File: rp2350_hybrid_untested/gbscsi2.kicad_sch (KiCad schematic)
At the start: 154 parts, among them J1 USB_DATA, J2 TF003, J3 Conn_01x02, J4 Conn_01x04, J5 SCSI_50-2P_2mm, J6 SCSI_50P_2.54mm, J7 Conn_01x04, Q1 AO3401A, Q10 AO3401A, Q11 AO3401A, Q12 AO3401A, Q13 AO3401A, Q14 AO3401A, Q15 AO3401A, Q16 AO3401A, Q17 AO3401A, Q18 AO3401A, Q2 AO3401A, Q3 AO3401A, Q4 AO3401A, Q5 AO3401A, Q6 AO3401A, Q7 AO3401A, Q8 AO3401A, Q9 AO3401A, SW1 SW_DIP_x04, U1 RP2350_60QFN, U2 W25Q128JVS, U4 74AHCT1G125, U7 AZ1117-2.85, U8 AP62250WU, U9 USB TVS, Y1 12MHz

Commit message: Changed diodes in BoM, minor corrections to PCB, documentation
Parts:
- D? (x4): LCSC C8598 -> C82544
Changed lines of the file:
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@@
       (effects (font (size 1.27 1.27)))
     )
-    (property "LCSC" "C8598" (at 281.94 27.94 0)
+    (property "LCSC" "C82544" (at 281.94 27.94 0)
       (effects (font (size 1.27 1.27)) hide)
     )
@@
       (effects (font (size 1.27 1.27)))
     )
-    (property "LCSC" "C8598" (at 274.32 35.56 0)
+    (property "LCSC" "C82544" (at 274.32 35.56 0)
       (effects (font (size 1.27 1.27)) hide)
     )
@@
       (effects (font (size 1.27 1.27)))
     )
-    (property "LCSC" "C8598" (at 281.94 57.15 0)
+    (property "LCSC" "C82544" (at 281.94 57.15 0)
       (effects (font (size 1.27 1.27)) hide)
     )
@@
       (effects (font (size 1.27 1.27)))
     )
-    (property "LCSC" "C8598" (at 281.94 66.04 0)
+    (property "LCSC" "C82544" (at 281.94 66.04 0)
       (effects (font (size 1.27 1.27)) hide)
     )

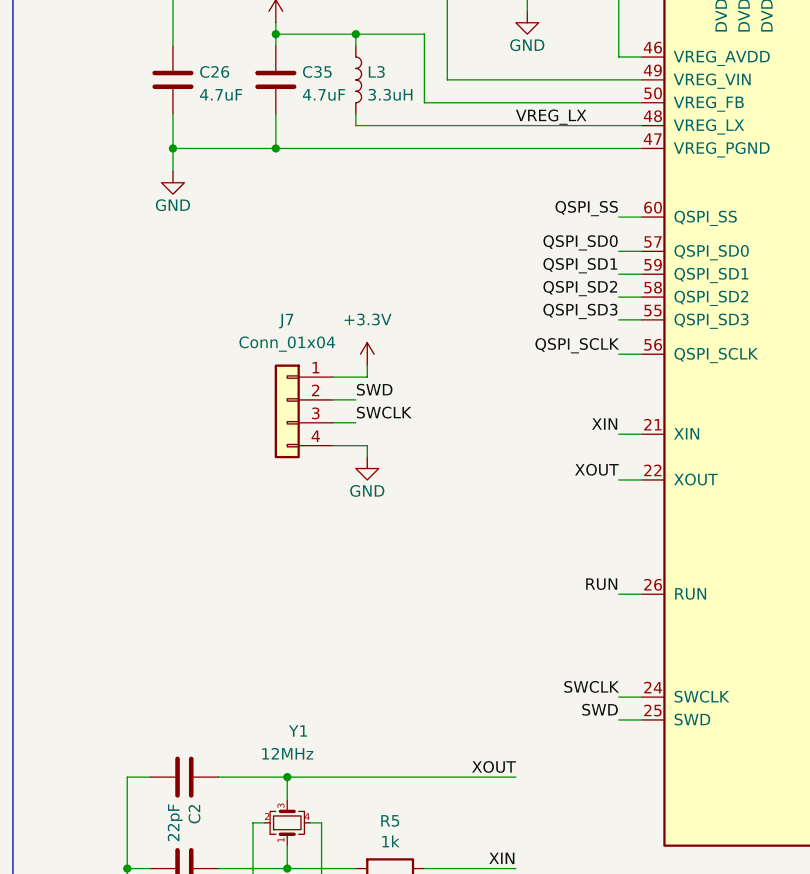
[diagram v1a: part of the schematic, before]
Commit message: BoM fixes for discrete variants, interactive BoMs added to each major type, mfg files for 2350
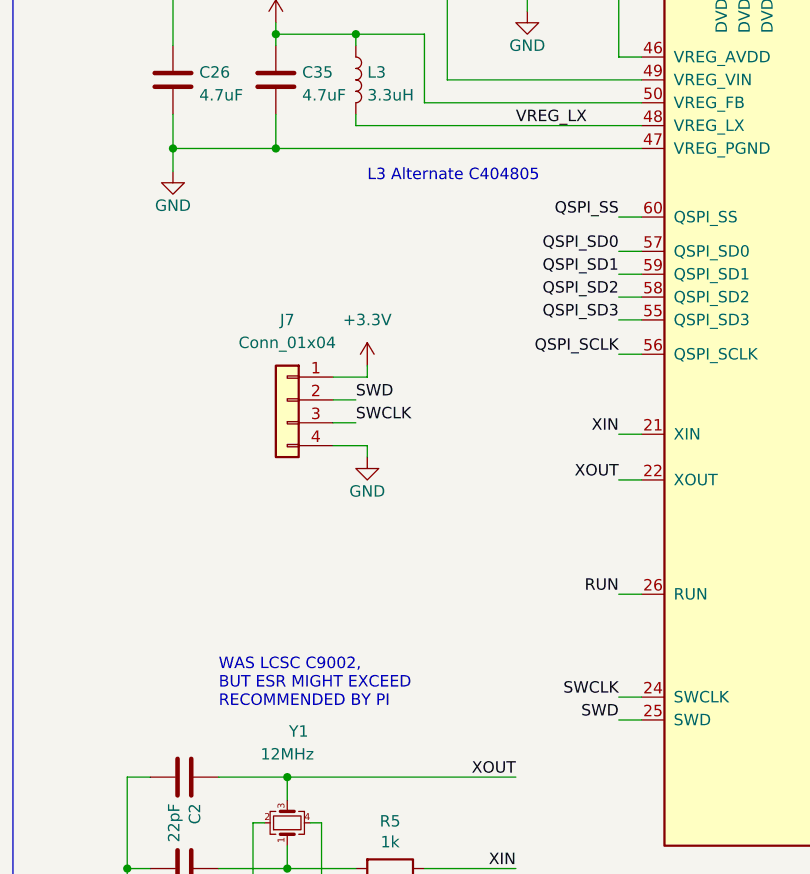
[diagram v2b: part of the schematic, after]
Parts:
- C1, C? (x10): LCSC Part # (none) -> C14663
- C10, C8: LCSC Part # (none) -> C52923
- C11, C12, C13, C14, C15, C16, C33, C36, C5, C6, C7: LCSC Part # (none) -> C307331
- C19: LCSC Part # (none) -> C346200
- C2, C3: LCSC Part # (none) -> C1555
- C26, C35: LCSC Part # (none) -> C23733
- C? (x2): LCSC Part # (none) -> C59461
- C? (x3): LCSC Part # (none) -> C15849
- C?: LCSC Part # (none) -> C38523
- C?: LCSC Part # (none) -> C96446
- D1, D6: LCSC Part # (none) -> C72038
- D? (x4): LCSC Part # (none) -> C82544
- F1, F2: LCSC Part # (none) -> C468888
- FID1, FID2, FID3, H1, H2, H3, H4, J3, J4, J5, J6, J7, JP3, R44: LCSC Part # (none) -> N/A
- J1: LCSC Part # (none) -> C165948
- J2: LCSC Part # (none) -> C5155563
- L2: LCSC Part # (none) -> C540967
- L3: LCSC Part # (none) -> C222831
- L?: LCSC Part # (none) -> C1002
- Q1, Q10, Q11, Q12, Q13, Q14, Q15, Q16, Q17, Q18, Q2, Q3, Q4, Q5, Q6, Q7, Q8, Q9: LCSC Part # (none) -> C15127
- R1, R5: LCSC C21190 -> C11702; LCSC Part # (none) -> C11702
- R22, R23, R24, R25, R26, R27, R28, R29, R30, R31, R32, R33, R34, R35, R36, R37, R38, R39, R?: LCSC Part # (none) -> C22781
- R3, R4: LCSC Part # (none) -> C25092
- R45: LCSC Part # (none) -> C21189
- R50, R52: LCSC Part # (none) -> C23193
- R? (x7): LCSC Part # (none) -> C21190
- R? (x15): LCSC Part # (none) -> C23162
- R?: LCSC Part # (none) -> C25967
- R?: LCSC Part # (none) -> C26083
- R? (x2): LCSC Part # (none) -> C25905
- R?: LCSC Part # (none) -> C25804
- SW1: LCSC Part # (none) -> C5160841
- U1: LCSC N/A -> C9900136995; LCSC Part # (none) -> C9900136995
- U2: LCSC Part # (none) -> C97521
- U4: LCSC Part # (none) -> C12494
- U7: LCSC Part # (none) -> C14791
- U8: LCSC Part # (none) -> C5184228
- U9: LCSC Part # (none) -> C2827654
- U? (x2): LCSC Part # (none) -> C2652121
- U? (x10): LCSC Part # (none) -> C7042
- Y1: LCSC C9002 -> C133334; LCSC Part # (none) -> C133334
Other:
- note added: "L3 Alternate C404805"
- note added: "WAS LCSC C9002, BUT ESR MIGHT EXCEED RECOMMENDED BY PI"
